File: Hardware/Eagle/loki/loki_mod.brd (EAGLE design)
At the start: 21.9 x 22.9 mm, 36 parts

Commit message: Update the watch application to support the Loki module.
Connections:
- net OSC2/RA6: now also 1H.5H
- net PGC/LED_M7: now also 10H.3K
- net RB1/LED_M6: now also 1H.8K
- net RB4/LED_H4: now also 10M.3K
- net RC3/LED_M4: now also 1M.8K
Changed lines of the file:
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@@
 <via x="13.6652" y="17.272" extent="1-16" drill="0.3048"/>
 <via x="8.001" y="8.763" extent="1-16" drill="0.3048"/>
+<contactref element="10M" pad="3K"/>
+<wire x1="12.065" y1="10.5918" x2="13.6506" y2="11.1046" width="0" layer="19" extent="1-16"/>
 </signal>
 <signal name="RC3/LED_M4">
@@
 <wire x1="14.478" y1="6.096" x2="15.1638" y2="6.096" width="0.1524" layer="1"/>
 <wire x1="19.0754" y1="11.1252" x2="19.0862" y2="11.13" width="0.1524" layer="1"/>
+<contactref element="1M" pad="8K"/>
+<wire x1="19.0862" y1="11.13" x2="19.0862" y2="18.03" width="0" layer="19" extent="1-1"/>
 </signal>
 <signal name="RC4/LED_M3">
@@
 <via x="1.016" y="16.3068" extent="1-16" drill="0.3048"/>
 <via x="5.6642" y="8.3058" extent="1-16" drill="0.3048"/>
+<contactref element="10H" pad="3K"/>
+<wire x1="1.9558" y1="12.0142" x2="2.8048" y2="11.1046" width="0" layer="19" extent="1-16"/>
 </signal>
 <signal name="PGD/RB7">
@@
 <via x="9.017" y="10.3124" extent="1-16" drill="0.3048"/>
 <via x="10.7696" y="10.3886" extent="1-16" drill="0.3048"/>
+<contactref element="1H" pad="8K"/>
+<wire x1="8.215" y1="11.1046" x2="8.215" y2="18.0046" width="0" layer="19" extent="1-1"/>
 </signal>
 <signal name="RA1/SW3">
@@
 <signal name="OSC2/RA6">
 <contactref element="U$1" pad="7"/>
+<contactref element="1H" pad="5H"/>
+<wire x1="13.3858" y1="3.048" x2="10.415" y2="11.1046" width="0" layer="19" extent="1-1"/>
 </signal>
 <signal name="RA5/SW4">

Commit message: Updated Loki board file.
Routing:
- net OSC2/RA6: track 0.00 -> 24.7 mm, vias 0 -> 2
- net RB3/LED_H3: track 29.5 -> 15.5 mm, vias 4 -> 2
- net N$2: track 35.7 -> 24.4 mm
- net RB1/LED_M6: track 4.57 -> 13.2 mm
- net RB2/LED_H2: track 12.1 -> 20.7 mm, vias 2 -> 4
- net T1OSI: track 36.0 -> 28.2 mm
- net N$9: track 33.6 -> 26.2 mm, vias 5 -> 4
- net RC3/LED_M4: track 8.67 -> 16.0 mm, vias 0 -> 2
- net VDD: track 68.4 -> 74.4 mm
- net PGC/LED_M7: track 16.3 -> 21.5 mm, vias 2 -> 7
- net RC6/LED_M1: track 18.6 -> 14.4 mm
- net RC4/LED_M3: track 20.8 -> 16.7 mm, vias 6 -> 4
- net N$10: track 25.6 -> 21.6 mm
- net GND: track 74.1 -> 70.2 mm, vias 5 -> 4
- net N$13: track 38.4 -> 42.1 mm, vias 9 -> 5
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
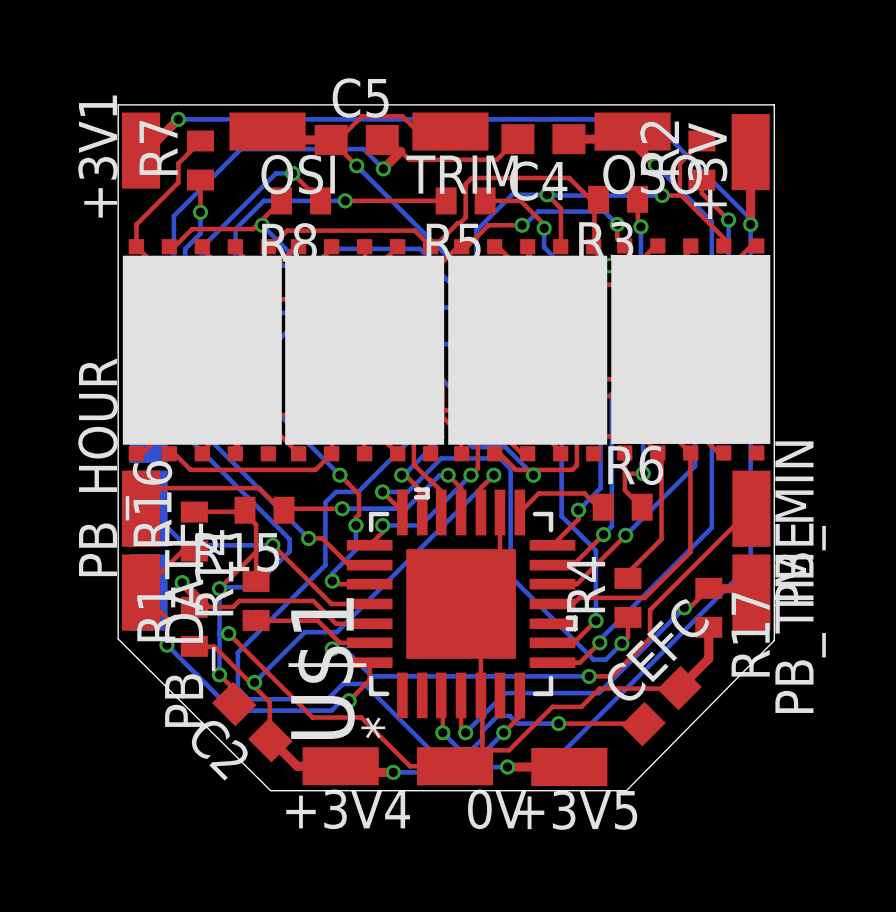
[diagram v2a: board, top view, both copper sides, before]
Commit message: Added resitor for date dot, if using the USSR replacement made display.
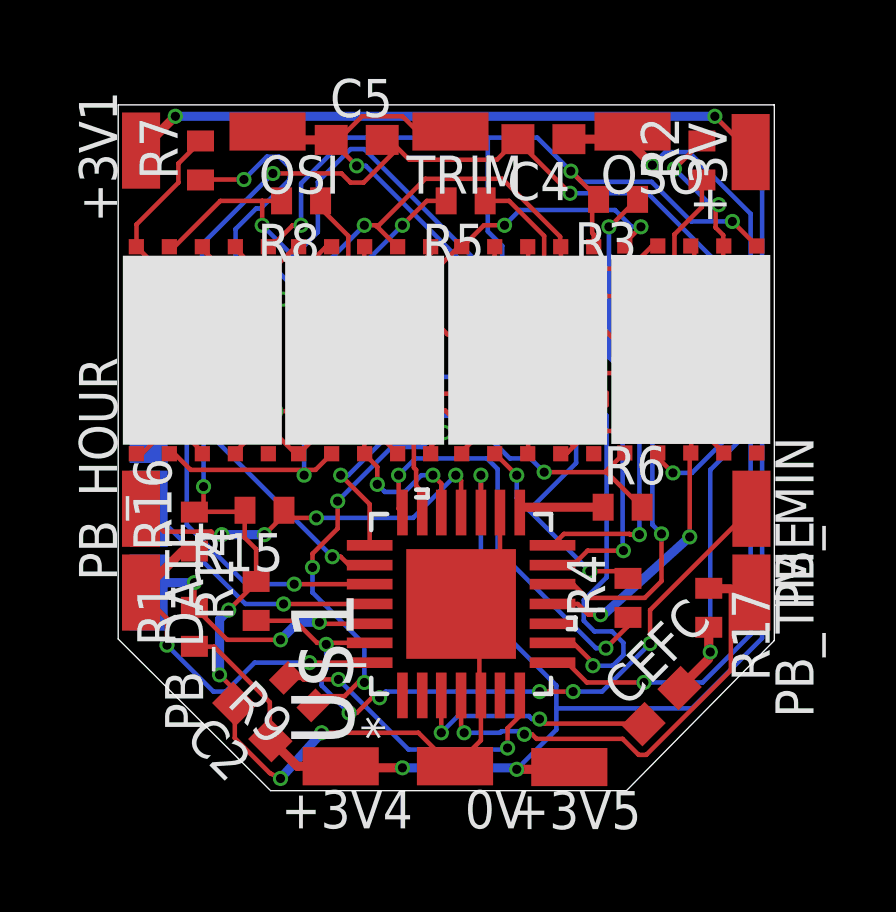
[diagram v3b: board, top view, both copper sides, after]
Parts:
- added R9: 120, resistor:R0402
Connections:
- new net N$1: 1H.5H, R9.1
- net OSC2/RA6: now also R9.2; no longer 1H.5H
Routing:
- net N$1: track 0.00 -> 14.5 mm, vias 0 -> 4
- net OSC2/RA6: track 24.7 -> 10.3 mm
- net N$10: track 21.6 -> 35.9 mm, vias 2 -> 4
- net N$13: track 42.1 -> 29.9 mm, vias 5 -> 11
- net N$7: track 28.8 -> 39.3 mm, vias 2 -> 6
- net N$8: track 30.9 -> 21.6 mm, vias 7 -> 4
- net RB2/LED_H2: track 20.7 -> 12.4 mm, vias 4 -> 2
- net GND: track 70.2 -> 77.3 mm, vias 4 -> 10
- net N$3: track 22.9 -> 29.7 mm, vias 5 -> 4
- net T1OSO: track 23.8 -> 29.6 mm
- net RB4/LED_H4: track 15.2 -> 20.2 mm, vias 6 -> 2
- net RB5/LED_H1: track 16.3 -> 20.4 mm
- net T1OSI: track 28.2 -> 32.0 mm
- net RA5/SW4: track 12.9 -> 15.9 mm
- net PGC/LED_M7: track 21.5 -> 19.1 mm, vias 7 -> 3
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
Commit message: Increased TRACE and VIA width were possible.
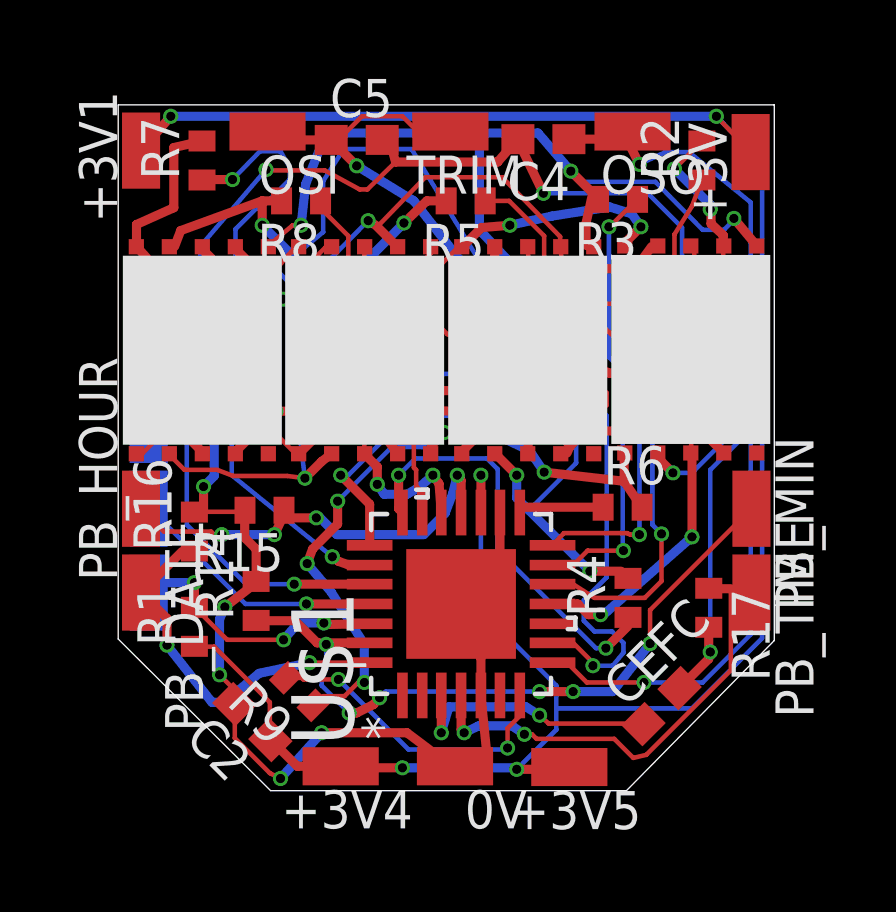
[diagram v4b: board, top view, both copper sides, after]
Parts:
- moved R7 0.05 mm to (2.79, 20.9)
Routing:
- net GND: track 77.3 -> 79.6 mm
- net N$10: track 35.9 -> 37.3 mm
- net N$3: track 29.7 -> 30.8 mm
- net RB0/SW2: track 13.4 -> 14.5 mm
- net N$2: track 26.0 -> 26.6 mm
- net N$7: track 39.3 -> 39.8 mm

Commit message: Added alarm decimal point.
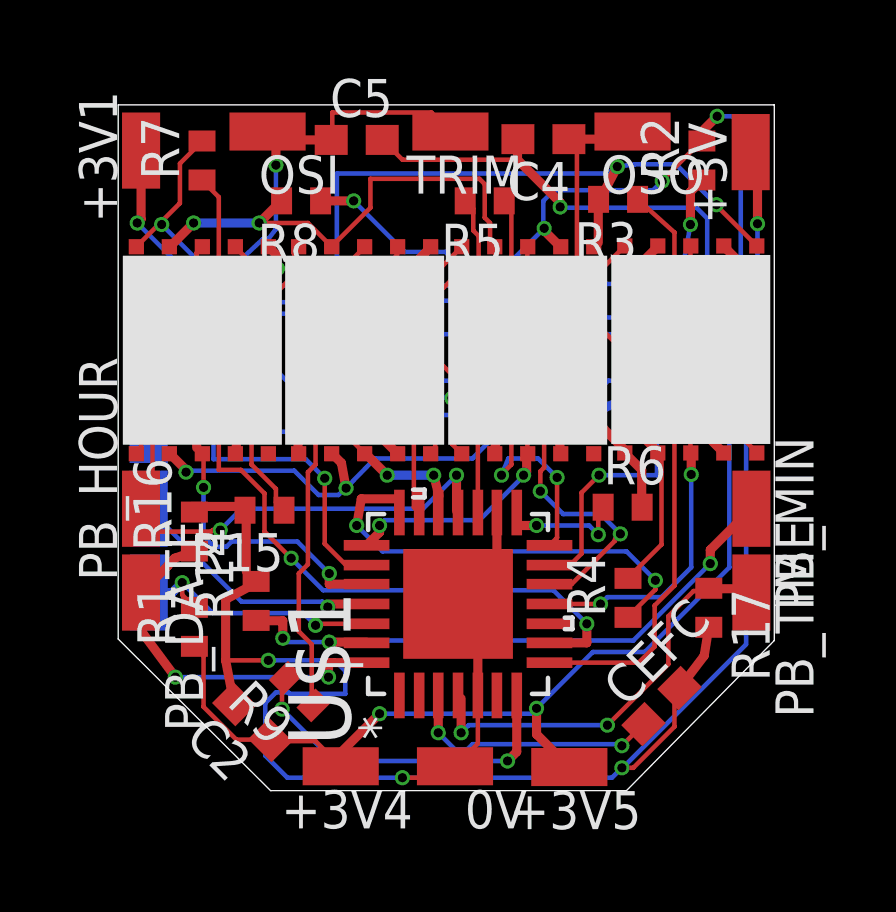
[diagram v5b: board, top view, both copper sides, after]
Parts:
- moved R5 0.63 mm to (12.2, 19.5)
- moved U$1 0.10 mm to (11.3, 6.10)
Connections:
- net N$1: now also 1M.5H
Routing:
- net N$1: track 14.5 -> 30.0 mm, vias 4 -> 3
- net N$7: track 39.8 -> 24.9 mm, vias 6 -> 4
- net RB0/SW2: track 14.5 -> 27.1 mm
- net N$10: track 37.3 -> 27.6 mm
- net N$3: track 30.8 -> 23.1 mm
- net RB4/LED_H4: track 20.2 -> 14.0 mm
- net N$8: track 21.8 -> 27.6 mm
- net T1OSI: track 32.0 -> 36.8 mm
- net T1OSO: track 29.8 -> 25.6 mm
- net RA0/SW1: track 23.8 -> 20.5 mm, vias 6 -> 3
- net VDD: track 74.8 -> 71.6 mm
- net RB5/LED_H1: track 20.5 -> 17.5 mm
- net RC4/LED_M3: track 18.0 -> 20.7 mm, vias 2 -> 4
- net GND: track 79.6 -> 82.2 mm, vias 10 -> 6
- net RC6/LED_M1: track 16.8 -> 14.4 mm
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
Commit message: Improved layout of Loki board using USSR made replacement display.
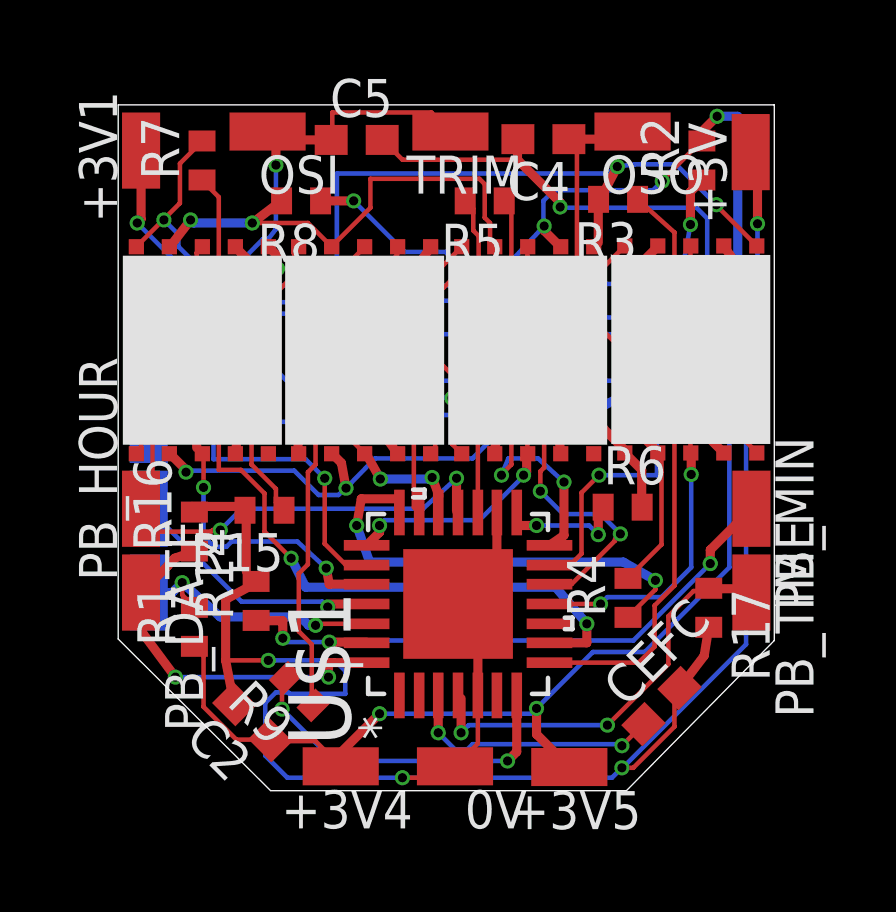
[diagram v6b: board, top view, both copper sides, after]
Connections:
- new net PIEZO: U$1.10
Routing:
- net N$9: track 28.9 -> 30.1 mm

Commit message: Optimized layout for manual soldering.
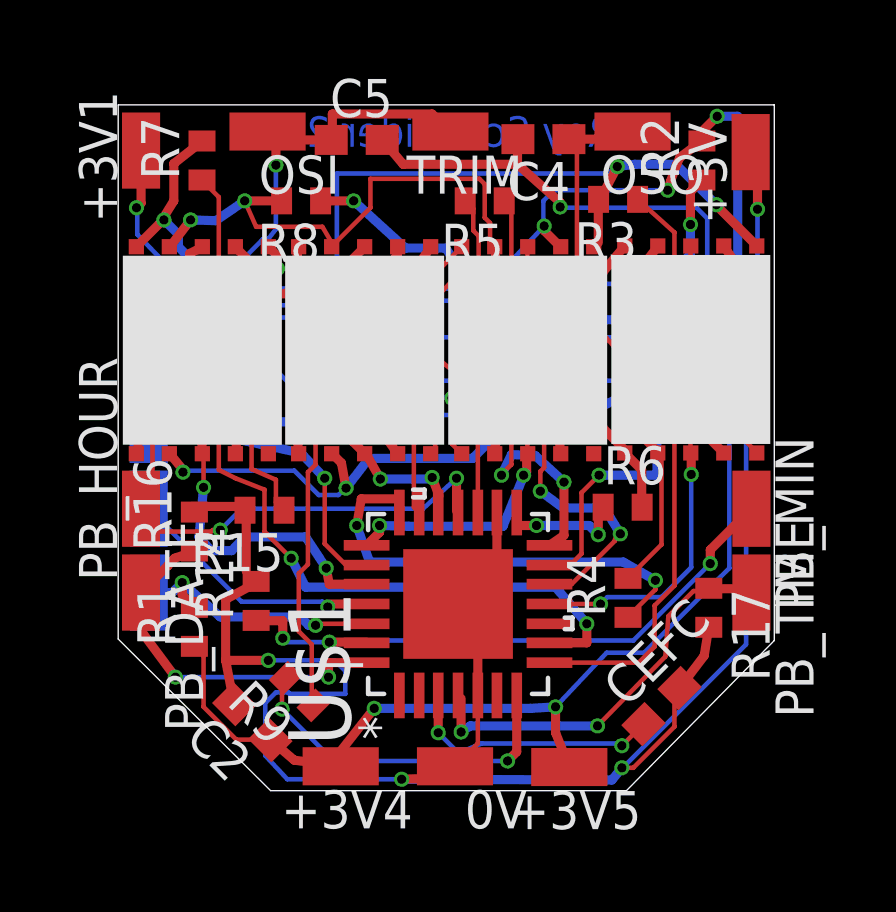
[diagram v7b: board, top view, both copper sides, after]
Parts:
- R2, R3, R4, R5, R6, R7, R8, R9: value 120 -> 105
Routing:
- net N$3: track 23.5 -> 24.4 mm
- net RB5/LED_H1: track 17.5 -> 16.8 mm
- net PGC/LED_M7: track 17.9 -> 18.5 mm
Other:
- board text added: "Roy Schneider 2020"

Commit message: Added the buzzer solder pad for the 'Loki' board.
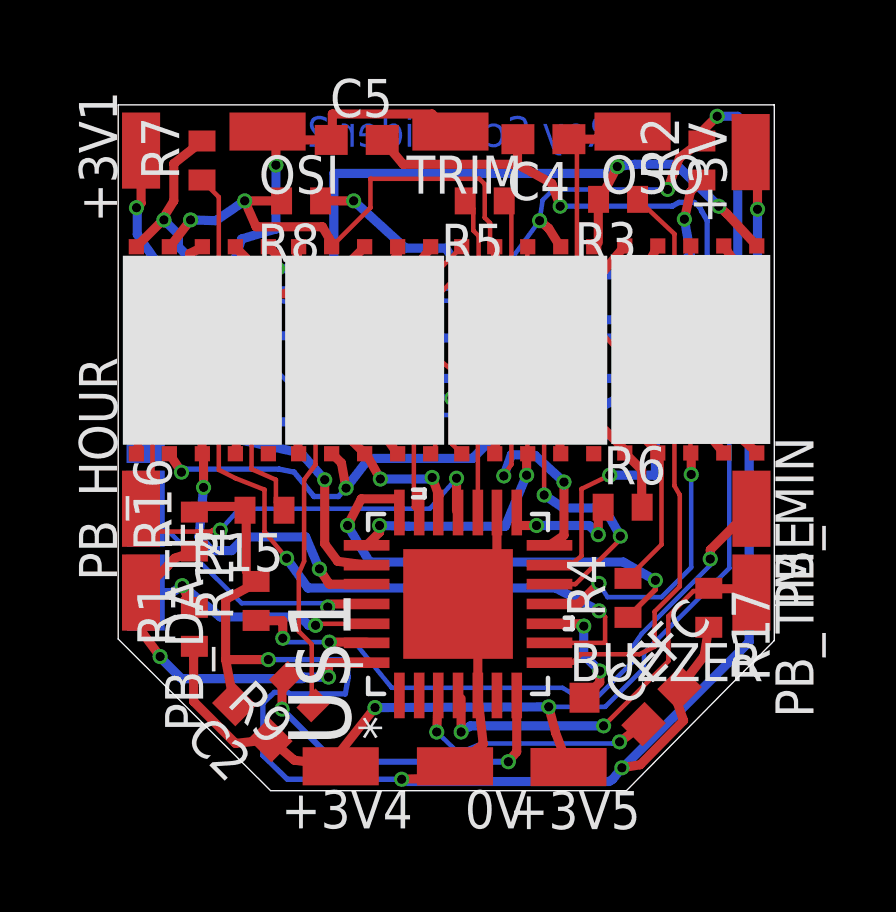
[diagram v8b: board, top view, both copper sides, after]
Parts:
- added BUZZER: TPSQTP10SQ, testpad:TP10SQ
- moved PAD1 0.10 mm to (0.91, 12.1)
- moved PAD2 0.10 mm to (0.91, 9.27)
- moved PAD5 0.10 mm to (0.91, 6.48)
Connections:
- net PIEZO: now also BUZZER.TP
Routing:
- net PIEZO: track 0.00 -> 3.99 mm, vias 0 -> 2
- net RA0/SW1: track 20.5 -> 22.4 mm
- net T1OSI: track 36.9 -> 38.2 mm
- net GND: track 82.5 -> 83.6 mm
- net VDD: track 71.6 -> 72.2 mm
